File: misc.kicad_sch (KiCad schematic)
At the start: 99 parts, among them CN2 Expansion, CN3 Cartridge, CN5 1P, CN504 AV Out, CN6 1P, CN7 Barrel_Jack, IC601 74ACT241, IC701 PIC16F630/18324, IC901 TL974, J2 EXT, Q1 MMBT3904, U1 TPS564257DRLR

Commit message: Add RGB amp from 3BP.
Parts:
- added C951, C952, C953, C954, C960: 100nF, Capacitor_SMD:C_0805_2012Metric, symbol Device:C
- added C961: 10uF, Capacitor_SMD:C_0805_2012Metric, symbol Device:C
- added IC951: THS7374, Package_SO:TSSOP-14_4.4x5mm_P0.65mm, symbol Amplifier_Video:THS7374
- added JP1: LPF, Jumper:SolderJumper-2_P1.3mm_Open_RoundedPad1.0x1.5mm, symbol Jumper:SolderJumper_2_Open
- added R826 (x5), R831: 5.62K, Resistor_SMD:R_0805_2012Metric, symbol Device:R
- added R831 (x3): 1.00K, Resistor_SMD:R_0805_2012Metric, symbol Device:R
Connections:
- net AVCC: now also C960.1, C961.2, IC951.10 (V_{S+}), JP1.2 (B)
- net GND: now also C960.2, C961.1, IC951.5 (GND), IC951.6 (DISABLE), R826.1, R831.2, R831.2, R831.2, R831.2
- net VIDEO_B: now also R50.2, R826.1; no longer R52.2
- net VIDEO_G: now also R826.1
- net VIDEO_R: now also R52.2, R826.1; no longer R50.2
- net ~{CSYNC}: now also R826.1; no longer FB7.1
- new net: C951.1, R826.2, R831.1
- new net: C951.2, IC951.1 (CH1_IN)
- new net: C954.2, IC951.2 (CH2_IN)
- new net: C953.2, IC951.3 (CH3_IN)
- new net: C952.2, IC951.4 (CH4_IN)
- new net: IC951.9 (BYPASS), JP1.1 (A), R826.2
- new net: C952.1, R826.2, R831.1
- new net: C954.1, R826.2, R831.1
- new net: C953.1, R826.2, R831.1
- new net 3BP_VIDEO_B: IC951.11 (CH4_OUT)
- new net 3BP_VIDEO_G: IC951.12 (CH3_OUT)
- new net 3BP_VIDEO_R: IC951.13 (CH2_OUT)
- new net ~{3BP_CSYNC}: FB7.1, IC951.14 (CH1_OUT)
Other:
- moved on the sheet: C10, C45, C701, CN504, FB1, FB7, IC701, J2, LED701, NF502, OSC1, R48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

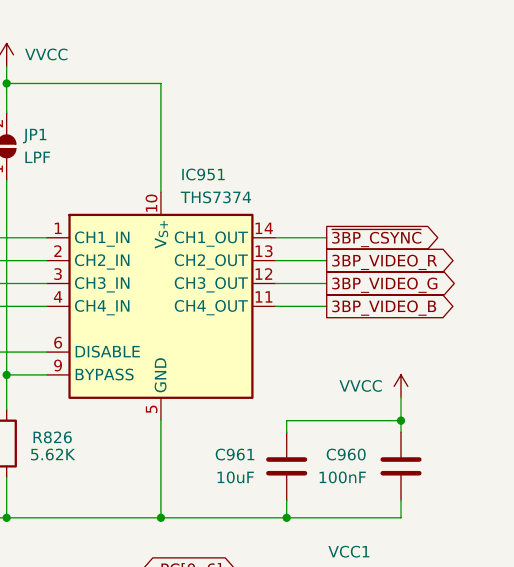
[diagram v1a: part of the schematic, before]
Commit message: Fix RGB swap, general tidying.
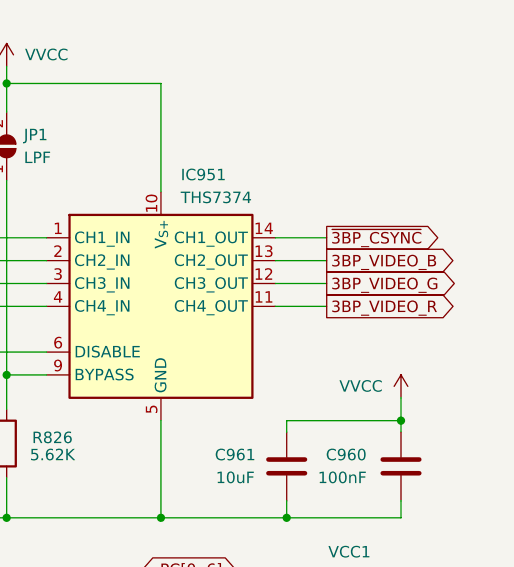
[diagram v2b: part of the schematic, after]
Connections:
- net 3BP_VIDEO_B: now also IC951.13 (CH2_OUT); no longer IC951.11 (CH4_OUT)
- net 3BP_VIDEO_R: now also IC951.11 (CH4_OUT); no longer IC951.13 (CH2_OUT)
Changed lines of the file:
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@@
     )
   )
-  (global_label "3BP_VIDEO_R" (shape output) (at 387.985 128.27 0) (fields_autoplaced)
+  (global_label "3BP_VIDEO_R" (shape output) (at 387.985 133.35 0) (fields_autoplaced)
     (effects (font (size 1.27 1.27)) (justify left))
-    (property "Intersheetrefs" "${INTERSHEET_REFS}" (at 403.3678 128.27 0)
+    (property "Intersheetrefs" "${INTERSHEET_REFS}" (at 403.3678 133.35 0)
       (effects (font (size 1.27 1.27)) (justify left) hide)
     )
@@
     )
   )
-  (global_label "3BP_VIDEO_B" (shape output) (at 387.985 133.35 0) (fields_autoplaced)
+  (global_label "3BP_VIDEO_B" (shape output) (at 387.985 128.27 0) (fields_autoplaced)
     (effects (font (size 1.27 1.27)) (justify left))
-    (property "Intersheetrefs" "${INTERSHEET_REFS}" (at 403.3678 133.35 0)
+    (property "Intersheetrefs" "${INTERSHEET_REFS}" (at 403.3678 128.27 0)
       (effects (font (size 1.27 1.27)) (justify left) hide)
     )
@@
         )
         (path "/bcc23b51-b742-4ae5-9dd6-d96a24058944/01513199-62c5-4123-a151-ccd381a5e6c1"
-          (reference "R695") (unit 1)
-        )
-      )
+          (reference "R965") (unit 1)
+        )
+      )

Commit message: Jumpers for RGB LPF.
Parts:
- removed JP1: LPF, Jumper:SolderJumper-2_P1.3mm_Open_RoundedPad1.0x1.5mm, symbol Jumper:SolderJumper_2_Open
- added R826: Fit to enable, Resistor_SMD:R_0805_2012Metric, symbol Device:R
- R826: value 5.62K -> Fit to disable
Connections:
- net AVCC: now also R826.2
- net GND: now also R826.1; no longer R826.1
- net LPF_BYPASS: now reaches IC951.9 (BYPASS)
- net LPF_BYPASS: now also R826.1, R826.2; no longer R826.2
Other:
- moved on the sheet: CE15, CE603, CN504, D1, FB7, IC901D, J2, NF502, R601, R602, R65, R66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

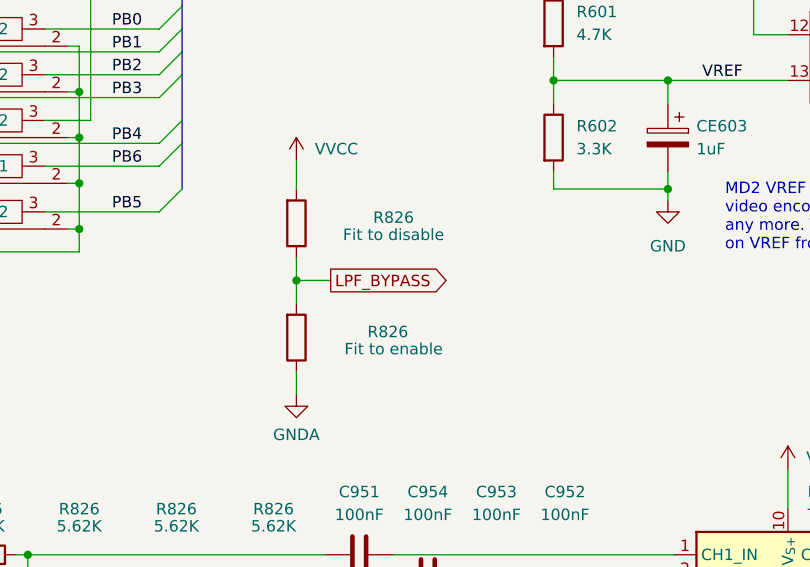
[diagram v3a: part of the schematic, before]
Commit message: Spec resistors for RGB LPF to avoid accidental short.
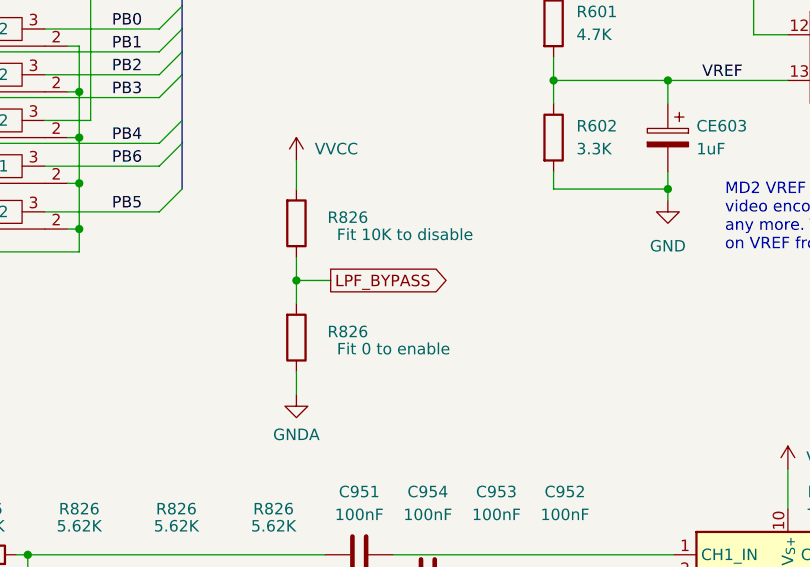
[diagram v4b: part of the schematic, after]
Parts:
- R826: value Fit to disable -> Fit 10K to disable
- R826: value Fit to enable -> Fit 0 to enable
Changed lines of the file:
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@@
   (symbol (lib_id "Device:R") (at 314.96 88.9 0) (mirror x) (unit 1)
     (in_bom yes) (on_board yes) (dnp no)
-    (property "Reference" "R826" (at 325.755 88.265 0)
-      (effects (font (size 1.27 1.27)))
-    )
-    (property "Value" "Fit to disable" (at 325.755 90.17 0)
+    (property "Reference" "R826" (at 320.675 88.265 0)
+      (effects (font (size 1.27 1.27)))
+    )
+    (property "Value" "Fit 10K to disable" (at 327.025 90.17 0)
       (effects (font (size 1.27 1.27)))
     )
@@
         )
         (path "/bcc23b51-b742-4ae5-9dd6-d96a24058944/01513199-62c5-4123-a151-ccd381a5e6c1"
-          (reference "J900") (unit 1)
+          (reference "R965") (unit 1)
         )
       )
@@
   (symbol (lib_id "Device:R") (at 314.96 101.6 0) (mirror x) (unit 1)
     (in_bom yes) (on_board yes) (dnp no)
-    (property "Reference" "R826" (at 325.12 100.965 0)
-      (effects (font (size 1.27 1.27)))
-    )
-    (property "Value" "Fit to enable" (at 325.755 102.87 0)
+    (property "Reference" "R826" (at 320.675 100.965 0)
+      (effects (font (size 1.27 1.27)))
+    )
+    (property "Value" "Fit 0 to enable" (at 325.755 102.87 0)
       (effects (font (size 1.27 1.27)))
     )
@@
         )
         (path "/bcc23b51-b742-4ae5-9dd6-d96a24058944/01513199-62c5-4123-a151-ccd381a5e6c1"
-          (reference "J901") (unit 1)
-        )
-      )
+          (reference "R966") (unit 1)
+        )
+      )

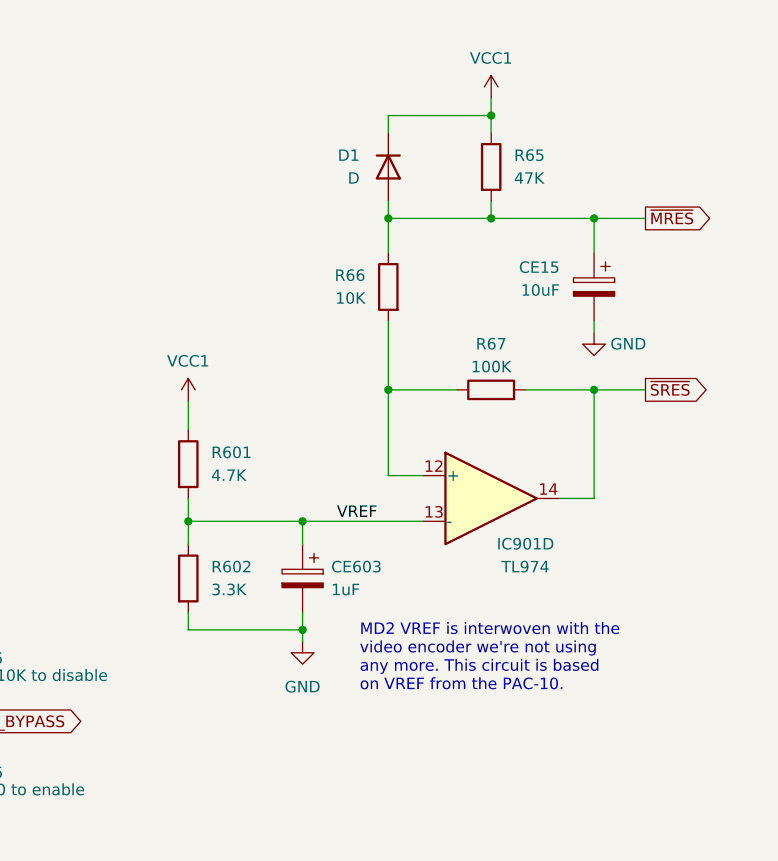
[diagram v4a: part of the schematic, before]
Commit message: Use 32X reset(s) for MD side.
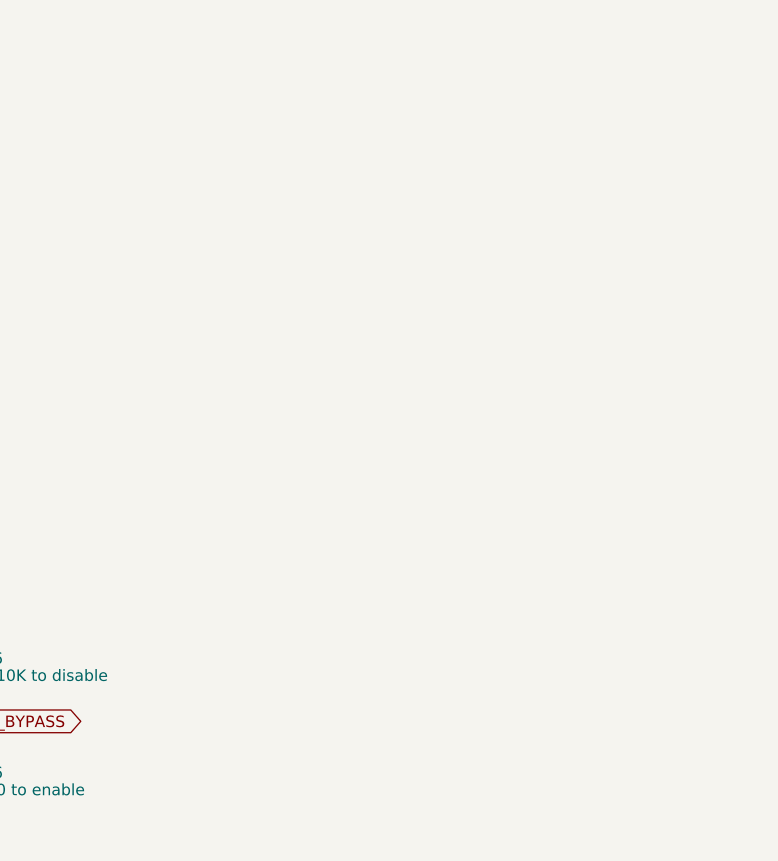
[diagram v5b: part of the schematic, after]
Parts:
- removed CE15: 10uF, Capacitor_THT:CP_Radial_D5.0mm_P2.50mm, symbol Device:C_Polarized
- removed CE603: 1uF, Capacitor_THT:CP_Radial_D5.0mm_P2.50mm, symbol Device:C_Polarized
- removed D1: D, Diode_THT:D_T-1_P5.08mm_Horizontal, symbol Device:D
- removed IC901: TL974, Package_SO:SO-14_3.9x8.65mm_P1.27mm, symbol Amplifier_Operational:TL064
- removed R601: 4.7K, Resistor_SMD:R_0805_2012Metric, symbol Device:R
- removed R602: 3.3K, Resistor_SMD:R_0805_2012Metric, symbol Device:R
- removed R65: 47K, Resistor_SMD:R_0805_2012Metric, symbol Device:R
- removed R66: 10K, Resistor_SMD:R_0805_2012Metric, symbol Device:R
- removed R67: 100K, Resistor_SMD:R_0805_2012Metric, symbol Device:R
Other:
- note removed: "MD2 VREF is interwoven with the video encoder we're not using any more. This circuit is based on VREF from the PAC-10."

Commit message: Remove mono audio, switch to 2-unit opamp.
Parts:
- removed FB7: 0, Inductor_SMD:L_0805_2012Metric, symbol Device:FerriteBead_Small
- removed R82, R83: 0, Resistor_SMD:R_0805_2012Metric, symbol Device:R
- added TP3: +5V, Connector_PinHeader_2.54mm:PinHeader_1x01_P2.54mm_Vertical, symbol Connector:TestPoint_Alt
- R1: value 30k -> 30K
- R2: value 162k -> 130K
- R5: value 10k -> 10K
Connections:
- net AVCC: now also TP3.1
- net ~{ASEL}: now also CN2.a22 (Pin_a22)
- net ~{RAS2}: now also CN2.a23 (Pin_a23)
- no-connect marks 9 -> 10
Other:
- note added: "Integrated 3BP RGB Amp"
- note added: "The THS7374 is not strictly necessary; its RGB inputs may indeed be passed as-is to the 32X encoder. It does however terminate the MD RGB signals allowing these to be fed to the encoder with the correct impedence."
- moved on the sheet: C10, C45, C951, C952, C953, C954, C960, C961, FB1, IC951, OSC1, R48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

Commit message: Footprint improvements, general tidying.
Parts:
- added TP4: ~{YS}, TestPoint:TestPoint_Pad_D1.5mm, symbol Connector:TestPoint
- C601: value 22nF -> 100nF
- D801: value 3A RECT -> 2A RECT
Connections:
- new net ~{YS}: TP4.1
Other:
- note added: "Test point for 32X bypass"
- moved on the sheet: C10, C45, CN5, CN6, EM11, EM12, EM13, EM14, EM15, EM16, EM17, EM18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

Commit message: Added LCSC Part # for some of the bird seed
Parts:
- C1: LCSC Part # (none) -> C2432124
- C10: LCSC Part # (none) -> C2237165
- C2, C3, C4, C5, C7, C8: LCSC Part # (none) -> C76666
- C44, C45: LCSC Part # (none) -> C2224419
- C595: LCSC Part # (none) -> C2232364
- C6: LCSC Part # (none) -> C2360979
- C60: LCSC Part # (none) -> C2230620
- C601, C701, C951, C952, C953, C954, C960: LCSC Part # (none) -> C2237864
- C9: LCSC Part # (none) -> C2246113
- C961: LCSC Part # (none) -> C342712
- FB1: LCSC Part # (none) -> C2441367
- FB7: LCSC Part # (none) -> C91037
- R1, R4: LCSC Part # (none) -> C844838
- R2, R5, R701: LCSC Part # (none) -> C844937
- R2, R611: LCSC Part # (none) -> C2077067
- R2: LCSC Part # (none) -> C1881352
- R3: LCSC Part # (none) -> C2079854
- R48: LCSC Part # (none) -> C3008897
- R50, R51, R52: LCSC Part # (none) -> C844634
- R68, R69, R70, R71: LCSC Part # (none) -> C844839
- R702: LCSC Part # (none) -> C844204
- R826, R831: LCSC Part # (none) -> C2131058
- R831: LCSC Part # (none) -> C844939
